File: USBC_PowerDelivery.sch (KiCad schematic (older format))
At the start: 33 parts, among them J1 Conn_02x06_Odd_Even, J2 Screw_Terminal_01x02, J3 1-2295018-2, Q1 AON7752, U1 STUSB4500QTR

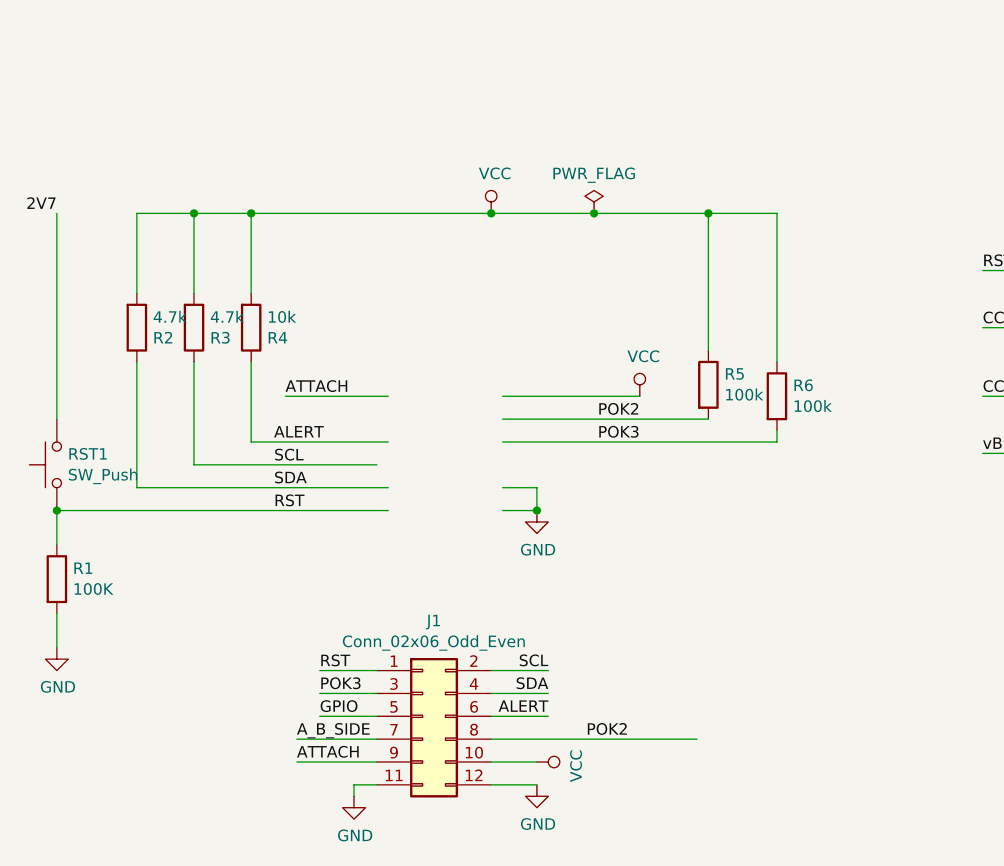
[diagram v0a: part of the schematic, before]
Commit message: added 3d fotprints and cleanup on schematic
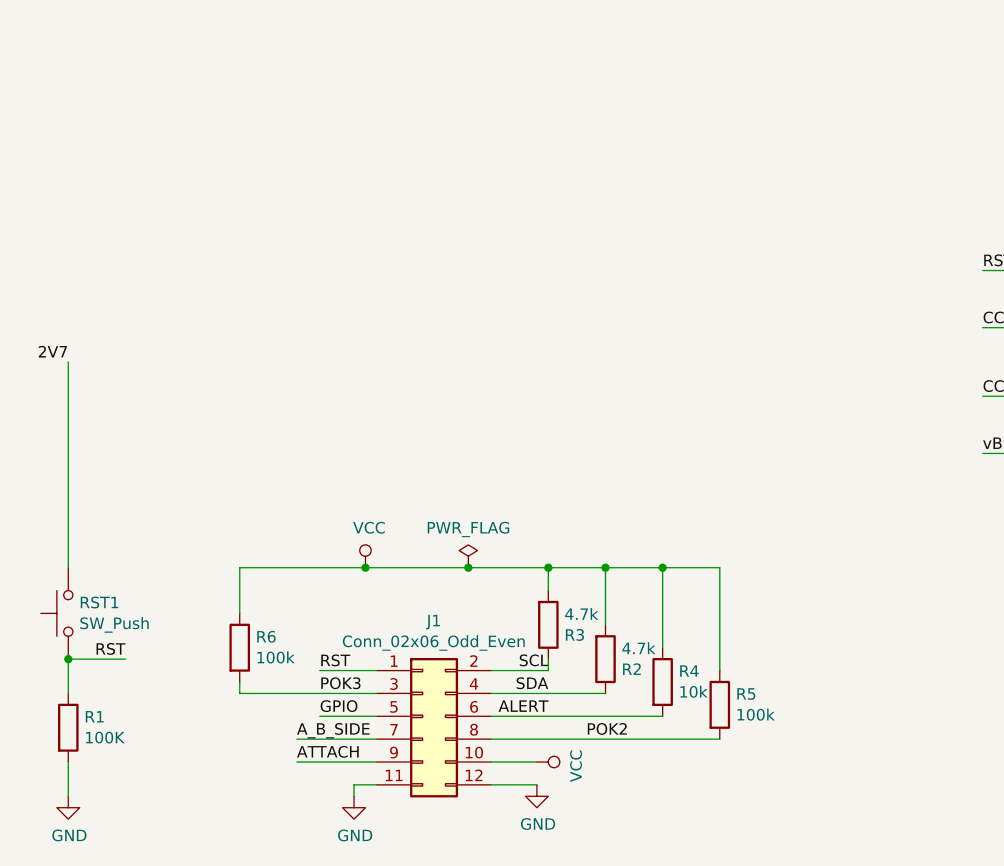
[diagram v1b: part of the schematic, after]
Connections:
- wire segments 121 -> 109
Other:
- moved on the sheet: R1, R2, R3, R4, R5, R6, RST1
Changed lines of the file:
@@
 L Device:R R1
 U 1 1 5DCF5937
-P 1000 4800
-F 0 "R1" H 1070 4846 50  0000 L CNN
-F 1 "100K" H 1070 4755 50  0000 L CNN
-F 2 "Resistor_SMD:R_0805_2012Metric" V 930 4800 50  0001 C CNN
-F 3 "~" H 1000 4800 50  0001 C CNN
-	1    1000 4800
+P 1050 5450
+F 0 "R1" H 1120 5496 50  0000 L CNN
+F 1 "100K" H 1120 5405 50  0000 L CNN
+F 2 "Resistor_SMD:R_0805_2012Metric" V 980 5450 50  0001 C CNN
+F 3 "~" H 1050 5450 50  0001 C CNN
+	1    1050 5450
 	1    0    0    -1
 $EndComp
@@
 Wire Wire Line
 	6300 3250 6300 3050
-Text Label 1950 4500 0    50   ~ 0
+Text Label 1300 5150 2    50   ~ 0
 RST
 $Comp
 L power:GND #PWR0116
 U 1 1 5DD8355C
-P 1000 5100
-F 0 "#PWR0116" H 1000 4850 50  0001 C CNN
-F 1 "GND" H 1005 4927 50  0000 C CNN
-F 2 "" H 1000 5100 50  0001 C CNN
-F 3 "" H 1000 5100 50  0001 C CNN
-	1    1000 5100
-	1    0    0    -1
-$EndComp
-Wire Wire Line
-	1000 4950 1000 5100
-Wire Wire Line
-	1000 4650 1000 4500
+P 1050 5750
+F 0 "#PWR0116" H 1050 5500 50  0001 C CNN
+F 1 "GND" H 1055 5577 50  0000 C CNN
+F 2 "" H 1050 5750 50  0001 C CNN
+F 3 "" H 1050 5750 50  0001 C CNN
+	1    1050 5750
+	1    0    0    -1
+$EndComp
+Wire Wire Line
+	1050 5600 1050 5750
+Wire Wire Line
+	1050 5300 1050 5150
 Text Label 7350 4550 2    50   ~ 0
 A_B_SIDE
@@
 L Device:R R4
 U 1 1 5DD94977
-P 1850 3700
-F 0 "R4" H 1920 3746 50  0000 L CNN
-F 1 "10k" H 1920 3655 50  0000 L CNN
-F 2 "Resistor_SMD:R_0805_2012Metric" V 1780 3700 50  0001 C CNN
-F 3 "~" H 1850 3700 50  0001 C CNN
-	1    1850 3700
-	1    0    0    1
-$EndComp
-Text Label 2000 4000 0    50   ~ 0
-ATTACH
+P 3650 5250
+F 0 "R4" H 3720 5296 50  0000 L CNN
+F 1 "10k" H 3720 5205 50  0000 L CNN
+F 2 "Resistor_SMD:R_0805_2012Metric" V 3580 5250 50  0001 C CNN
+F 3 "~" H 3650 5250 50  0001 C CNN
+	1    3650 5250
+	1    0    0    -1
+$EndComp
 Text Label 2150 5400 0    50   ~ 0
 GPIO
@@
 L Switch:SW_Push RST1
 U 1 1 5DDACAAD
-P 1000 4300
-F 0 "RST1" V 1046 4252 50  0000 R CNN
-F 1 "SW_Push" V 955 4252 50  0000 R CNN
-F 2 "Button_Switch_SMD:SW_SPST_EVQPE1" H 1000 4500 50  0001 C CNN
-F 3 "~" H 1000 4500 50  0001 C CNN
-	1    1000 4300
+P 1050 4950
+F 0 "RST1" V 1096 4902 50  0000 R CNN
+F 1 "SW_Push" V 1005 4902 50  0000 R CNN
+F 2 "Button_Switch_SMD:SW_SPST_EVQPE1" H 1050 5150 50  0001 C CNN
+F 3 "~" H 1050 5150 50  0001 C CNN
+	1    1050 4950
 	0    -1   -1   0
 $EndComp
-Connection ~ 1000 4500
 Text Label 2050 5500 0    50   ~ 0
 A_B_SIDE
 Wire Wire Line
 	2050 5500 2400 5500
-Wire Wire Line
-	2000 4000 2450 4000
-Text Label 1950 4200 0    50   ~ 0
-ALERT
 Text Label 3150 5200 2    50   ~ 0
 SCL
@@
 L Device:R R3
 U 1 1 5DDDA43E
-P 1600 3700
-F 0 "R3" H 1670 3746 50  0000 L CNN
-F 1 "4.7k" H 1670 3655 50  0000 L CNN
-F 2 "Resistor_SMD:R_0805_2012Metric" V 1530 3700 50  0001 C CNN
-F 3 "~" H 1600 3700 50  0001 C CNN
-	1    1600 3700
+P 3150 5000
+F 0 "R3" H 3220 5046 50  0000 L CNN
+F 1 "4.7k" H 3220 4955 50  0000 L CNN
+F 2 "Resistor_SMD:R_0805_2012Metric" V 3080 5000 50  0001 C CNN
+F 3 "~" H 3150 5000 50  0001 C CNN
+	1    3150 5000
 	1    0    0    1
 $EndComp
@@
 L Device:R R2
 U 1 1 5DDDA5F0
-P 1350 3700
-F 0 "R2" H 1420 3746 50  0000 L CNN
-F 1 "4.7k" H 1420 3655 50  0000 L CNN
-F 2 "Resistor_SMD:R_0805_2012Metric" V 1280 3700 50  0001 C CNN
-F 3 "~" H 1350 3700 50  0001 C CNN
-	1    1350 3700
+P 3400 5150
+F 0 "R2" H 3470 5196 50  0000 L CNN
+F 1 "4.7k" H 3470 5105 50  0000 L CNN
+F 2 "Resistor_SMD:R_0805_2012Metric" V 3330 5150 50  0001 C CNN
+F 3 "~" H 3400 5150 50  0001 C CNN
+	1    3400 5150
 	1    0    0    1
 $EndComp
-Wire Wire Line
-	2450 4400 1350 4400
-Wire Wire Line
-	1350 4400 1350 3850
-Wire Wire Line
-	1600 4300 1600 3850
-Wire Wire Line
-	2450 4200 1850 4200
-Wire Wire Line
-	1850 4200 1850 3850
-Wire Wire Line
-	2950 4000 3550 4000
 Text Label 5400 4450 0    50   ~ 0
 SCL
@@
 Text Label 5400 4650 0    50   ~ 0
 ALERT
-Text Label 3550 4100 2    50   ~ 0
-POK2
-Text Label 3550 4200 2    50   ~ 0
-POK3
 $Comp
 L Device:R R5
 U 1 1 5DDF7310
-P 3850 3950
-F 0 "R5" H 3920 3996 50  0000 L CNN
-F 1 "100k" H 3920 3905 50  0000 L CNN
-F 2 "Resistor_SMD:R_0805_2012Metric" V 3780 3950 50  0001 C CNN
-F 3 "~" H 3850 3950 50  0001 C CNN
-	1    3850 3950
+P 3900 5350
+F 0 "R5" H 3970 5396 50  0000 L CNN
+F 1 "100k" H 3970 5305 50  0000 L CNN
+F 2 "Resistor_SMD:R_0805_2012Metric" V 3830 5350 50  0001 C CNN
+F 3 "~" H 3900 5350 50  0001 C CNN
+	1    3900 5350
 	1    0    0    -1
 $EndComp
@@
 L Device:R R6
 U 1 1 5DDF7940
-P 4150 4000
-F 0 "R6" H 4220 4046 50  0000 L CNN
-F 1 "100k" H 4220 3955 50  0000 L CNN
-F 2 "Resistor_SMD:R_0805_2012Metric" V 4080 4000 50  0001 C CNN
-F 3 "~" H 4150 4000 50  0001 C CNN
-	1    4150 4000
-	1    0    0    -1
-$EndComp
-Wire Wire Line
-	4150 4200 4150 4150
-Wire Wire Line
-	2950 4200 4150 4200
-Wire Wire Line
-	2950 4100 3850 4100
-Wire Wire Line
-	3850 3800 3850 3200
-Wire Wire Line
-	4150 3850 4150 3200
-Wire Wire Line
-	4150 3200 3850 3200
-Wire Wire Line
-	1350 3200 1350 3550
-Connection ~ 3850 3200
-Wire Wire Line
-	1600 3550 1600 3200
-Connection ~ 1600 3200
-Wire Wire Line
-	1600 3200 1350 3200
-Wire Wire Line
-	1850 3550 1850 3200
-Connection ~ 1850 3200
-Wire Wire Line
-	1850 3200 1600 3200
-$Comp
-L power:GND #PWR0117
-U 1 1 5DE1B0C0
-P 3100 4500
-F 0 "#PWR0117" H 3100 4250 50  0001 C CNN
-F 1 "GND" H 3105 4327 50  0000 C CNN
-F 2 "" H 3100 4500 50  0001 C CNN
-F 3 "" H 3100 4500 50  0001 C CNN
-	1    3100 4500
-	1    0    0    -1
-$EndComp
-Wire Wire Line
-	2950 4400 3100 4400
+P 1800 5100
+F 0 "R6" H 1870 5146 50  0000 L CNN
+F 1 "100k" H 1870 5055 50  0000 L CNN
+F 2 "Resistor_SMD:R_0805_2012Metric" V 1730 5100 50  0001 C CNN
+F 3 "~" H 1800 5100 50  0001 C CNN
+	1    1800 5100
+	1    0    0    -1
+$EndComp
 $Comp
 L Device:LED D2
@@
 	1    0    0    -1
 $EndComp
-Wire Wire Line
-	1850 3200 2900 3200
 Connection ~ 6050 2100
 Wire Wire Line
 	6050 2100 6500 2100
-$Comp
-L power:VCC #PWR0119
-U 1 1 5DE5D092
-P 3550 4000
-F 0 "#PWR0119" H 3550 3850 50  0001 C CNN
-F 1 "VCC" H 3567 4173 50  0000 C CNN
-F 2 "" H 3550 4000 50  0001 C CNN
-F 3 "" H 3550 4000 50  0001 C CNN
-	1    3550 4000
-	1    0    0    -1
-$EndComp
 $Comp
 L power:VCC #PWR0120
 U 1 1 5DE61B9B
-P 2900 3200
-F 0 "#PWR0120" H 2900 3050 50  0001 C CNN
-F 1 "VCC" H 2917 3373 50  0000 C CNN
-F 2 "" H 2900 3200 50  0001 C CNN
-F 3 "" H 2900 3200 50  0001 C CNN
-	1    2900 3200
-	1    0    0    -1
-$EndComp
-Connection ~ 2900 3200
-Wire Wire Line
-	2900 3200 3350 3200
+P 2350 4750
+F 0 "#PWR0120" H 2350 4600 50  0001 C CNN
+F 1 "VCC" H 2367 4923 50  0000 C CNN
+F 2 "" H 2350 4750 50  0001 C CNN
+F 3 "" H 2350 4750 50  0001 C CNN
+	1    2350 4750
+	1    0    0    -1
+$EndComp
 Wire Wire Line
 	2150 5400 2400 5400
-Wire Wire Line
-	1000 4500 2450 4500
-Wire Wire Line
-	2950 4500 3100 4500
-Connection ~ 3100 4500
-Wire Wire Line
-	3100 4400 3100 4500
 $Comp
 L russian-nixies:1-2295018-2 J3
@@
 L power:PWR_FLAG #FLG0102
 U 1 1 5DF55113
-P 3350 3200
-F 0 "#FLG0102" H 3350 3275 50  0001 C CNN
-F 1 "PWR_FLAG" H 3350 3373 50  0000 C CNN
-F 2 "" H 3350 3200 50  0001 C CNN
-F 3 "~" H 3350 3200 50  0001 C CNN
-	1    3350 3200
-	1    0    0    -1
-$EndComp
-Connection ~ 3350 3200
-Wire Wire Line
-	3350 3200 3850 3200
+P 2800 4750
+F 0 "#FLG0102" H 2800 4825 50  0001 C CNN
+F 1 "PWR_FLAG" H 2800 4923 50  0000 C CNN
+F 2 "" H 2800 4750 50  0001 C CNN
+F 3 "~" H 2800 4750 50  0001 C CNN
+	1    2800 4750
+	1    0    0    -1
+$EndComp
 $Comp
 L power:PWR_FLAG #FLG0103
@@
 	9100 3150 9200 3150
 Wire Wire Line
-	1000 3200 1000 4100
+	1050 3850 1050 4750
 Text Label 2150 5200 0    50   ~ 0
 RST
@@
 	2150 5200 2400 5200
 Wire Wire Line
-	2900 5300 3150 5300
-Wire Wire Line
 	2900 5200 3150 5200
-Text Label 1950 4300 0    50   ~ 0
-SCL
-Wire Wire Line
-	1600 4300 2400 4300
-Text Label 1950 4400 0    50   ~ 0
-SDA
 Text Label 2150 5300 0    50   ~ 0
 POK3
@@
 Text Label 3150 5400 2    50   ~ 0
 ALERT
-Wire Wire Line
-	2900 5400 3150 5400
 Text Label 2050 5600 0    50   ~ 0
 ATTACH
@@
 	1    0    0    -1
 $EndComp
-Wire Wire Line
-	2400 5300 2150 5300
 Text Label 3500 5500 2    50   ~ 0
 POK2
 Wire Wire Line
-	2900 5500 3800 5500
+	2900 5500 3900 5500
 Wire Wire Line
 	2900 5600 3100 5600
@@
 	1    0    0    -1
 $EndComp
-Text Label 1000 3200 2    50   ~ 0
+Text Label 1050 3850 2    50   ~ 0
 2V7
+Wire Wire Line
+	1800 5300 1800 5250
+Wire Wire Line
+	1800 5300 2400 5300
+Wire Wire Line
+	1800 4950 1800 4750
+Wire Wire Line
+	1800 4750 2350 4750
+Connection ~ 2350 4750
+Wire Wire Line
+	2350 4750 2800 4750
+Wire Wire Line
+	1300 5150 1050 5150
+Connection ~ 1050 5150
+Wire Wire Line
+	2900 5400 3650 5400
+Wire Wire Line
+	2900 5300 3400 5300
+Wire Wire Line
+	3150 5150 3150 5200
+Wire Wire Line
+	3150 4850 3150 4750
+Wire Wire Line
+	3150 4750 2800 4750
+Connection ~ 2800 4750
+Wire Wire Line
+	3150 4750 3400 4750
+Wire Wire Line
+	3900 4750 3900 5200
+Connection ~ 3150 4750
+Wire Wire Line
+	3650 5100 3650 4750
+Connection ~ 3650 4750
+Wire Wire Line
+	3650 4750 3900 4750
+Wire Wire Line
+	3400 5000 3400 4750
+Connection ~ 3400 4750
+Wire Wire Line
+	3400 4750 3650 4750
 $EndSCHEMATC
